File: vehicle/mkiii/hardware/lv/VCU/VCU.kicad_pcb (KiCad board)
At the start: 2 copper layers, 0 parts

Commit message: Resolved some "footprint not exist" issues
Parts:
- added C1: C_0.1uF, OEM:C_0603_1608Metric, F.Cu at (99.6, 103.5)
- added C10: C_0.1uF, OEM:C_0603_1608Metric, F.Cu at (104.7, 67.2)
- added C11: C_10uF_10V, OEM:C_0603_1608Metric, F.Cu at (104.7, 69.7)
- added C12: C_0.1uF, OEM:C_0603_1608Metric, F.Cu at (104.7, 72.2)
- added C13: C_1uF, OEM:C_0603_1608Metric, F.Cu at (104.7, 74.7)
- added C14: C_0.1uF, OEM:C_0603_1608Metric, F.Cu at (104.7, 77.2)
- added C15: C_0.1uF, OEM:C_0603_1608Metric, F.Cu at (104.7, 79.7)
- added C16: C_0.1uF, OEM:C_0603_1608Metric, F.Cu at (104.7, 82.2)
- added C18: C_0.22uF_50V, OEM:C_0603_1608Metric, F.Cu at (130.1, 92.2)
- added C19: C_0.1uF, OEM:C_0603_1608Metric, F.Cu at (130.1, 94.7)
- added C2: C_10nF, OEM:C_0603_1608Metric, F.Cu at (99.6, 106.0)
- added C20: C_0.1uF, OEM:C_0603_1608Metric, F.Cu at (130.1, 97.2)
- added C21: C_1uF_25V, OEM:C_0603_1608Metric, F.Cu at (130.1, 99.7)
- added C22: C_0.1uF_16V, OEM:C_0603_1608Metric, F.Cu at (130.1, 102.2)
- added C23: C_0.1uF, OEM:C_0603_1608Metric, F.Cu at (134.1, 92.2)
- added C24: C_0.1uF, OEM:C_0603_1608Metric, F.Cu at (149.7, 92.2)
- added C25: C_0.1uF, OEM:C_0603_1608Metric, F.Cu at (149.7, 94.7)
- added C26: C_0.1uF_16V, OEM:C_0603_1608Metric, F.Cu at (103.6, 106.0)
- added C27: C_0.1uF, OEM:C_0603_1608Metric, F.Cu at (130.1, 80.2)
- added C28: C_0.1uF, OEM:C_0603_1608Metric, F.Cu at (103.6, 108.5)
- added C29: C_0.1uF, OEM:C_0603_1608Metric, F.Cu at (103.6, 111.0)
- added C3: C_0.1uF, OEM:C_0603_1608Metric, F.Cu at (99.6, 108.5)
- added C30: C_10uF_10V, OEM:C_0603_1608Metric, F.Cu at (130.1, 82.7)
- added C4: C_1uF, OEM:C_0603_1608Metric, F.Cu at (99.6, 111.0)
- added C5: C_4.7uF, OEM:C_0603_1608Metric, F.Cu at (99.6, 113.5)
- added C6: C_0.1uF, OEM:C_0603_1608Metric, F.Cu at (99.6, 116.1)
- added C7: C_30pF, OEM:C_0603_1608Metric, F.Cu at (99.6, 118.6)
- added C8: C_30pF, OEM:C_0603_1608Metric, F.Cu at (103.6, 103.5)
- added C9: C_10uF_10V, OEM:C_0603_1608Metric, F.Cu at (130.1, 77.6)
- added D1: MOTOR_ON, OEM:D_0805_2012Metric, F.Cu at (111.8, 113.4)
- added D10: D_36V_500mW, OEM:D_SOD-123, F.Cu at (105.6, 98.6)
- added D11: BSPD_TRIP_LED, OEM:D_0805_2012Metric, F.Cu at (122.5, 77.9)
- added D13: D_Blue_LED, OEM:D_0805_2012Metric, F.Cu at (139.5, 115.7)
- added D14: HEARTBEAT, OEM:D_0805_2012Metric, F.Cu at (120.7, 119.5)
- added D15: D_Blue_LED, OEM:D_0805_2012Metric, F.Cu at (139.5, 118.7)
- added D2: BRAKES, OEM:D_0805_2012Metric, F.Cu at (111.8, 116.5)
- added D3: BSPD_TRIP, OEM:D_0805_2012Metric, F.Cu at (111.8, 119.5)
- added D4: HEARTBEAT, OEM:D_0805_2012Metric, F.Cu at (116.3, 113.4)
- added D5: 5V, OEM:D_0805_2012Metric, F.Cu at (116.3, 116.5)
- added D6: 3V3, OEM:D_0805_2012Metric, F.Cu at (116.3, 119.5)
- added D7: MISO, OEM:D_0805_2012Metric, F.Cu at (120.7, 113.4)
- added D8: MOSI, OEM:D_0805_2012Metric, F.Cu at (120.7, 116.5)
- added D9: D_Amber_LED, OEM:D_0805_2012Metric, F.Cu at (122.5, 74.9)
- added F1: F_500mA_8V, OEM:Fuse_1206_3216Metric, F.Cu at (147.2, 78.0)
- added F2: F_500mA_8V, OEM:Fuse_1206_3216Metric, F.Cu at (147.2, 81.3)
- added H1: H_MountingHole, OEM:H_MountingHole, F.Cu at (140.3, 79.6)
- added J1: J_Programming_Pin_Header, OEM:J_Programming_Pin_Header_Keyed, F.Cu at (111.9, 104.5)
- added J2: J_PCIe_x1, OEM:J_PCIe_x1_Key, F.Cu at (129.8, 71.9)
- added K1: K_10A_5V, OEM:G5Q1A4DC5 (K_SPST-NO_10A_5V_TH - G5Q-1A4-DC5), F.Cu at (105.5, 94.0)
- added Q1: SSM3K333R,LF, OEM:SOT-23-3, F.Cu at (100.1, 68.3)
- added Q2: SSM3K333R,LF, OEM:SOT-23-3, F.Cu at (100.1, 73.0)
- added Q3: SSM3K333R,LF, OEM:SOT-23-3, F.Cu at (142.7, 105.3)
- added Q5: SSM3K333R,LF, OEM:SOT-23-3, F.Cu at (134.7, 116.6)
- added Q6: SSM3K333R,LF, OEM:SOT-23-3, F.Cu at (134.7, 121.2)
- added R1: R_200, OEM:R_0603_1608Metric, F.Cu at (103.6, 113.5)
- added R10: R_100k, OEM:R_0603_1608Metric, F.Cu at (108.7, 69.7)
- added R11: R_1k, OEM:R_0603_1608Metric, F.Cu at (108.7, 72.2)
- added R12: R_71.5k, OEM:R_0603_1608Metric, F.Cu at (108.7, 74.7)
- added R13: R_10k, OEM:R_0603_1608Metric, F.Cu at (108.7, 77.2)
- added R14: R_10k, OEM:R_0603_1608Metric, F.Cu at (108.7, 79.7)
- added R15: R_10k, OEM:R_0603_1608Metric, F.Cu at (108.7, 82.2)
- added R16: R_100k, OEM:R_0603_1608Metric, F.Cu at (112.7, 67.2)
- added R17: R_10k, OEM:R_0603_1608Metric, F.Cu at (112.7, 69.7)
- added R18: R_1k, OEM:R_0603_1608Metric, F.Cu at (112.7, 72.2)
- added R19: R_10k, OEM:R_0603_1608Metric, F.Cu at (112.7, 74.7)
- added R2: R_200, OEM:R_0603_1608Metric, F.Cu at (103.6, 116.1)
- added R21: R_75k, OEM:R_0603_1608Metric, F.Cu at (134.1, 94.7)
- added R22: R_576, OEM:R_0603_1608Metric, F.Cu at (134.1, 97.2)
- added R23: R_100, OEM:R_0603_1608Metric, F.Cu at (134.1, 99.7)
- added R24: R_10k, OEM:R_0603_1608Metric, F.Cu at (134.1, 102.2)
- added R25: R_1k, OEM:R_0603_1608Metric, F.Cu at (138.1, 92.2)
- added R26: R_10k, OEM:R_0603_1608Metric, F.Cu at (138.1, 94.7)
- added R27: R_10k, OEM:R_0603_1608Metric, F.Cu at (138.1, 97.2)
- added R28: R_10k, OEM:R_0603_1608Metric, F.Cu at (138.1, 99.7)
- added R3: R_200, OEM:R_0603_1608Metric, F.Cu at (103.6, 118.6)
- added R32: R_3k, OEM:R_0603_1608Metric, F.Cu at (130.1, 115.4)
- added R33: R_100k, OEM:R_0603_1608Metric, F.Cu at (130.1, 118.0)
- added R34: R_10k, OEM:R_0603_1608Metric, F.Cu at (130.1, 120.5)
- added R35: R_1M, OEM:R_0603_1608Metric, F.Cu at (149.7, 97.2)
- added R36: R_0, OEM:R_0603_1608Metric, F.Cu at (149.7, 99.7)
- added R37: R_2.2k, OEM:R_0603_1608Metric, F.Cu at (149.7, 102.2)
- added R38: R_1M, OEM:R_0603_1608Metric, F.Cu at (149.7, 104.7)
- added R39: R_120, OEM:R_0603_1608Metric, F.Cu at (107.6, 116.1)
- added R4: R_200, OEM:R_0603_1608Metric, F.Cu at (107.6, 103.5)
- added R40: R_0, OEM:R_0603_1608Metric, F.Cu at (149.7, 107.2)
- added R41: R_2.2k, OEM:R_0603_1608Metric, F.Cu at (149.7, 109.8)
- added R42: R_10k, OEM:R_0603_1608Metric, F.Cu at (130.1, 85.2)
- added R43: R_10k, OEM:R_0603_1608Metric, F.Cu at (130.1, 87.7)
- added R44: R_5.1k, OEM:R_0603_1608Metric, F.Cu at (134.1, 77.6)
- added R45: R_10k, OEM:R_0603_1608Metric, F.Cu at (134.1, 80.2)
- added R46: R_200, OEM:R_0603_1608Metric, F.Cu at (134.1, 82.7)
- added R47: R_5.1k, OEM:R_0603_1608Metric, F.Cu at (134.1, 85.2)
- added R48: R_10k, OEM:R_0603_1608Metric, F.Cu at (134.1, 87.7)
- added R49: R_200, OEM:R_0603_1608Metric, F.Cu at (107.6, 118.6)
- added R5: R_1k, OEM:R_0603_1608Metric, F.Cu at (107.6, 106.0)
- added R50: R_3k, OEM:R_0603_1608Metric, F.Cu at (130.1, 123.0)
- added R51: R_100k, OEM:R_0603_1608Metric, F.Cu at (130.1, 125.5)
- added R52: R_10k, OEM:R_0603_1608Metric, F.Cu at (130.1, 128.0)
- added R6: R_200, OEM:R_0603_1608Metric, F.Cu at (107.6, 108.5)
- added R7: R_200, OEM:R_0603_1608Metric, F.Cu at (107.6, 111.0)
- added R8: R_200, OEM:R_0603_1608Metric, F.Cu at (107.6, 113.5)
- added R9: R_100k, OEM:R_0603_1608Metric, F.Cu at (108.7, 67.2)
- added SW1: SW_0.05A_12V, OEM:B3U-1000P (SW_SPST_0.05A_12V_SMD - B3U-1000P), F.Cu at (122.8, 67.8)
- added SW2: SW_0.05A_12V, OEM:B3U-1000P (SW_SPST_0.05A_12V_SMD - B3U-1000P), F.Cu at (122.8, 71.5)
- added TP1: 5V, OEM:TP_Hook_SMD, F.Cu at (112.3, 123.0)
- added TP10: TP_SMD, OEM:TP_Hook_SMD, F.Cu at (154.4, 92.9)
- added TP11: TP_SMD, OEM:TP_Hook_SMD, F.Cu at (154.4, 96.9)
- added TP12: TP_SMD, OEM:TP_Hook_SMD, F.Cu at (134.9, 125.4)
- added TP2: GND, OEM:TP_Hook_SMD, F.Cu at (112.3, 127.0)
- added TP3: TP_SMD, OEM:TP_Hook_SMD, F.Cu at (117.5, 67.9)
- added TP4: TP_SMD, OEM:TP_Hook_SMD, F.Cu at (117.5, 71.9)
- added TP5: TP_SMD, OEM:TP_Hook_SMD, F.Cu at (117.5, 75.9)
- added TP6: TP_SMD, OEM:TP_Hook_SMD, F.Cu at (142.9, 92.9)
- added TP7: TP_SMD, OEM:TP_Hook_SMD, F.Cu at (142.9, 96.9)
- added TP8: TP_SMD, OEM:TP_Hook_SMD, F.Cu at (142.9, 100.9)
- added U1: STM32G441CBT6, OEM:LQFP-48_7x7mm_P0.5mm, F.Cu at (103.2, 125.5)
- added U10: MCP6001T-I/LT, OEM:SOT-353_SC-70-5, F.Cu at (153.8, 100.9)
- added U11: MCP6001T-I/LT, OEM:SOT-353_SC-70-5, F.Cu at (153.8, 104.9)
- added U12: MCP2561-E_SN, OEM:SOIC-8_3.9x4.9mm_P1.27mm, F.Cu at (119.3, 124.4)
- added U13: MCP6001T-I/LT, OEM:SOT-353_SC-70-5, F.Cu at (146.5, 85.0)
- added U2: SN74LVC1G08DBVR, OEM:SOT-23-5, F.Cu at (100.1, 77.6)
- added U3: MCP6001T-I/LT, OEM:SOT-353_SC-70-5, F.Cu at (122.4, 81.4)
- added U4: SN74LVC1G02DBVR, OEM:SOT-23-5, F.Cu at (100.1, 82.2)
- added U5: SN74LVC1G02DBVR, OEM:SOT-23-5, F.Cu at (100.1, 86.8)
- added U6: SN74LVC1G32DBVR, OEM:SOT-23-5, F.Cu at (142.7, 110.0)
- added U7: MCP6001T-I/LT, OEM:SOT-353_SC-70-5, F.Cu at (130.2, 105.5)
- added U8: MCP6001T-I/LT, OEM:SOT-353_SC-70-5, F.Cu at (130.2, 109.4)
- added Y1: X_16MHz_18pF, OEM:FA238160000MBC0 (X_16MHz_18pF_SMD - FA-238_16.0000MB-C0), F.Cu at (120.1, 105.2)
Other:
- board outline added: 20.3 x 8.4 mm

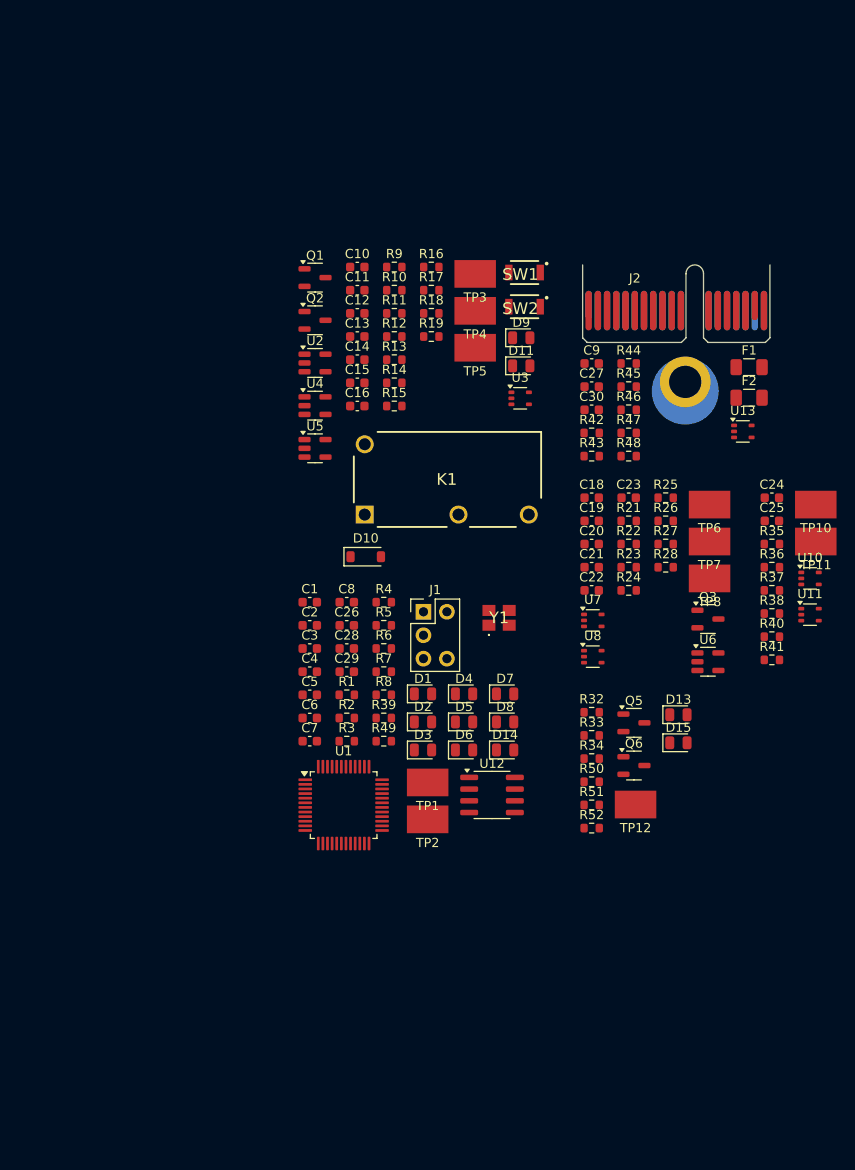
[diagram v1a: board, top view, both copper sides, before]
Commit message: Layout completed, review required
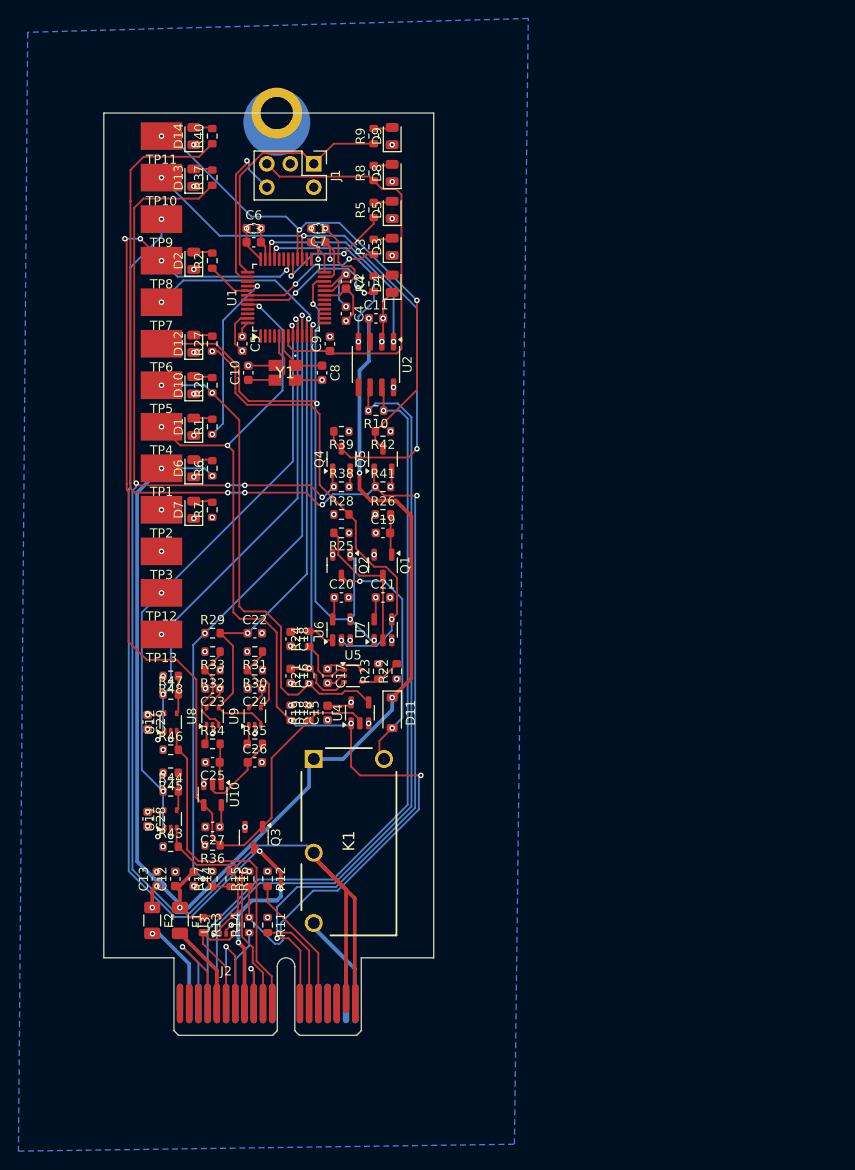
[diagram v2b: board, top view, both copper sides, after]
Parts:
- removed SW1, SW2: SW_0.05A_12V, OEM:B3U-1000P (SW_SPST_0.05A_12V_SMD - B3U-1000P)
- added TP11: TP_SMD, OEM:TP_Hook_SMD, F.Cu at (83.5, 53.0)
- added TP2: 3V3, OEM:TP_Hook_SMD, F.Cu at (83.5, 93.5)
- D5: renamed from D14; value HEARTBEAT -> THROTTLE_DISABLE
- D8: renamed from D7; value MISO -> NRST
- D9: renamed from D8; value MOSI -> SWDIO
- moved J2 87.2 mm to (85.5, 147.0)
- moved F1 86.0 mm to (85.5, 138.0), turned to -90 degrees
- moved F2 86.0 mm to (82.5, 138.0), turned to -90 degrees
- moved TP10 85.2 mm to (83.5, 57.5)
- moved D14 81.8 mm to (87.0, 53.0), turned to 90 degrees
- moved D13 80.7 mm to (87.0, 57.5), turned to 90 degrees
- moved U3 77.4 mm to (90.5, 138.5), turned to 90 degrees
- moved R37 77.3 mm to (89.0, 57.5), turned to 90 degrees
- moved C28 76.1 mm to (82.0, 127.0), turned to -90 degrees
- moved R40 74.8 mm to (89.0, 53.0), turned to 90 degrees
- moved U11 74.0 mm to (84.5, 127.0), turned to 90 degrees
- moved R43 72.9 mm to (84.5, 130.0)
- moved C12 71.8 mm to (85.0, 133.5), turned to 90 degrees
- moved TP13 71.6 mm to (83.5, 107.0)
- moved TP12 71.5 mm to (83.5, 102.5)
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- renumbered C29 to C1, C8 to C10, C26 to C11, C9 to C12, C30 to C13, C27 to C14, C10 to C15, C11 to C16, C12 to C17, C13 to C18, C14 to C19, C15 to C20, C16 to C21, C18 to C22, C19 to C23, C20 to C24, C21 to C25, C22 to C26, C23 to C27, C24 to C28, C25 to C29, C1 to C3, C3 to C5, C5 to C6, C28 to C7, C7 to C8, C6 to C9, D9 to D10, D10 to D11, D11 to D12, D15 to D13, D13 to D14, D5 to D6, D6 to D7, Q6 to Q4, R39 to R10, R45 to R11, R46 to R12, R42 to R13, R47 to R14, R48 to R15, R44 to R16, R43 to R17, R9 to R18, R10 to R19, R11 to R20, R12 to R21, R13 to R22, R14 to R23, R15 to R24, R16 to R25, R17 to R26, R18 to R27, R19 to R28, R21 to R29, R22 to R30, R23 to R31, R24 to R32, R25 to R33, R26 to R34, R27 to R35, R28 to R36, R50 to R37, R51 to R38, R52 to R39, R32 to R40, R33 to R41, R34 to R42, R35 to R43, R40 to R44, R41 to R45, R38 to R46, R36 to R47, R37 to R48, R49 to R5, R5 to R6, R6 to R7, R7 to R8, R8 to R9, TP12 to TP10, TP10 to TP12, TP11 to TP13, TP2 to TP3, TP3 to TP4, TP4 to TP5, TP5 to TP6, TP6 to TP7, TP7 to TP8, TP8 to TP9, U6 to U10, U10 to U11, U11 to U12, U12 to U2, U13 to U3, U2 to U4, U3 to U5, U4 to U6, U5 to U7, U7 to U8, U8 to U9
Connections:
- U1 pad 1: +3V3 -> unconnected-(U1-VBAT-Pad1)
- U1 pad 43: /Microcontroller - STM32G441CBT6 (page 2)/HEARTBEAT -> /Microcontroller - STM32G441CBT6 (page 2)/HEARTBEAT_LED
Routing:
- net /BSPD/BSPD_RELAY_OUT: track 0.00 -> 166.7 mm, vias 0 -> 5
- net +5V: track 0.00 -> 150.7 mm, vias 0 -> 6
- net /PCIe x1 Connector/SS_INERTIA_SWITCH: track 0.00 -> 145.2 mm, vias 0 -> 6
- net /BSPD/BRAKELIGHT_LL: track 0.00 -> 118.3 mm, vias 0 -> 4
- net /BSPD/MOTOR_CURRENT_SENSE: track 0.00 -> 115.7 mm, vias 0 -> 7
- net /BrakeLight/BRAKELIGHT_CONN: track 0.00 -> 114.4 mm, vias 0 -> 4
- net /Microcontroller - STM32G441CBT6 (page 2)/CAN_-: track 0.00 -> 85.3 mm, vias 0 -> 1
- net /Microcontroller - STM32G441CBT6 (page 2)/CAN_+: track 0.00 -> 82.7 mm, vias 0 -> 1
- net GND: track 0.00 -> 80.6 mm, vias 0 -> 69
- net /BrakeLight/BRAKE_PRESS_SENSE_FILTERED: track 0.00 -> 75.6 mm, vias 0 -> 3
- net /BSPD/BSPD_LL: track 0.00 -> 72.8 mm, vias 0 -> 5
- net /BrakeLight/BRAKE_PRESS_SENSE: track 0.00 -> 72.0 mm, vias 0 -> 3
- net /Microcontroller - STM32G441CBT6 (page 2)/OUTPUT_THROTTLE_1: track 0.00 -> 65.9 mm, vias 0 -> 4
- net /Microcontroller - STM32G441CBT6 (page 2)/BSPD_SHUTDOWN_SENSE: track 0.00 -> 62.6 mm, vias 0 -> 3
- net /Microcontroller - STM32G441CBT6 (page 2)/SS_INERTIA_OUTPUT: track 0.00 -> 57.2 mm, vias 0 -> 3
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- added copper zone on In2.Cu, net +3V3
- added copper zone on B.Cu, net GND
- added copper zone on In1.Cu, net GND
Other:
- board size 20.3 x 8.4 mm -> 35.8 x 91.6 mm
- copper layers 2 -> 4

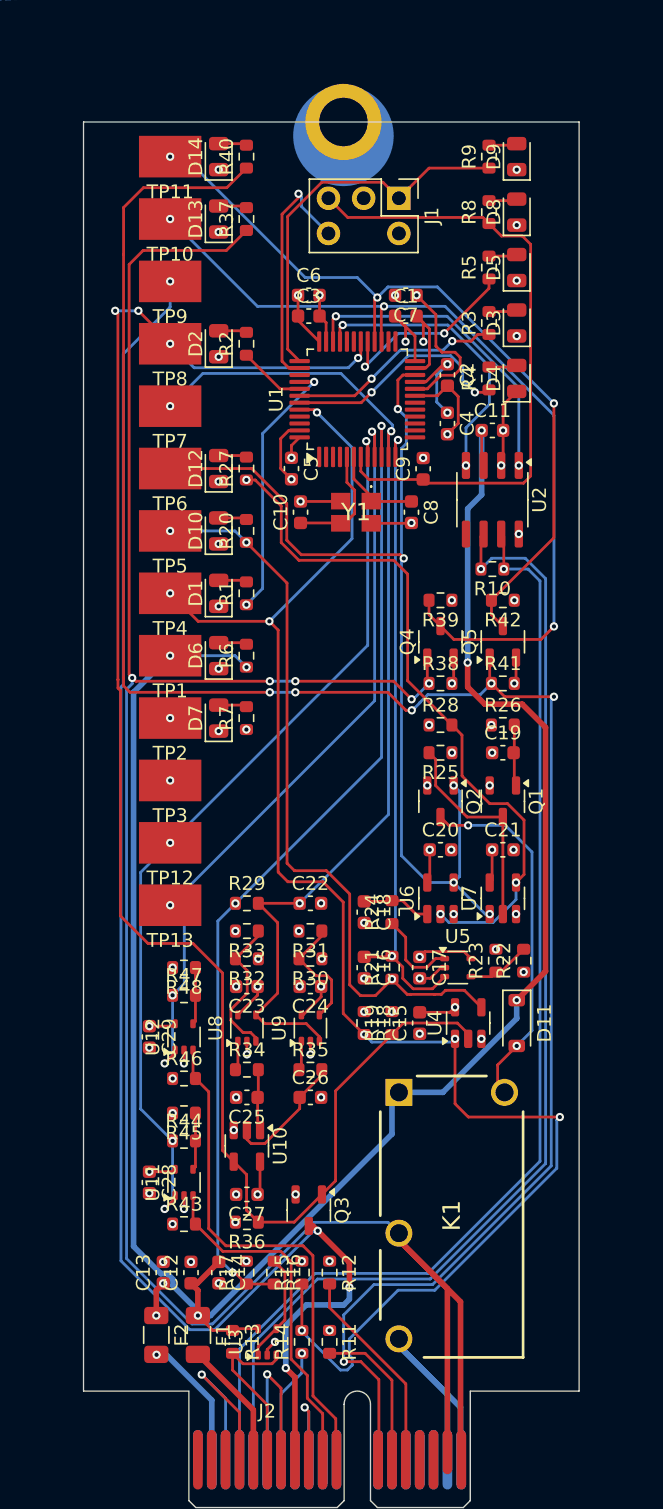
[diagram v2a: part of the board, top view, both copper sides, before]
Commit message: Final PCB layout after adding silkscreen and icon
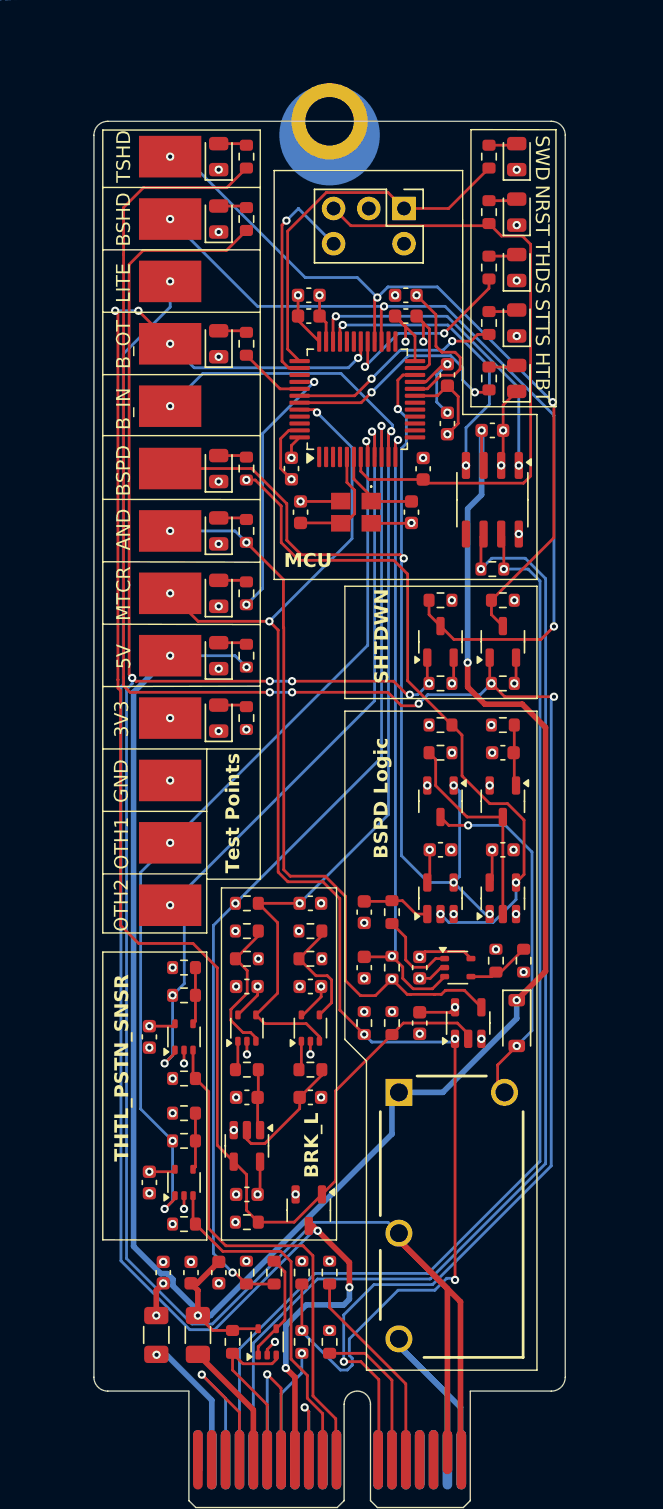
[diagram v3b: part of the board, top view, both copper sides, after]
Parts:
- added G***: LOGO, LOGO, B.Cu at (95.7, 75.1)
- moved H1 1.00 mm to (95.0, 50.4)
- moved J1 0.83 mm to (100.4, 56.7)
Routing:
- net /BSPD/MOTOR_CURRENT_SENSE: track 115.7 -> 106.1 mm
- net /Microcontroller - STM32G441CBT6 (page 2)/SWCLK: track 17.9 -> 16.6 mm
- net /Microcontroller - STM32G441CBT6 (page 2)/SWDIO: track 27.7 -> 27.1 mm
- net /Microcontroller - STM32G441CBT6 (page 2)/NRST: track 46.3 -> 45.7 mm
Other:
- board size 35.8 x 91.6 mm -> 34 x 91.6 mm
- board text added: "3V3"
- board text added: "5V"
- board text added: "AND"
- board text added: "BRK_L"
- board text added: "BSHD"
- board text added: "BSPD"
- board text added: "BSPD Logic"
- board text added: "B_IN"
- board text added: "B_OT"
- board text added: "GND"
- board text added: "HTBT"
- board text added: "LITE"
- board text added: "MCU"
- board text added: "MTCR"
- board text added: "NRST"
- board text added: "OTH1"
- board text added: "OTH2"
- board text added: "SHTDWN"
- board text added: "STTS"
- board text added: "SWD"
- board text added: "THDS"
- board text added: "THTL_PSTN_SNSR"
- board text added: "TSHD"
- board text added: "Test Points"

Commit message: Minor ERC Fixes in Schematics; Minor Silkscreen Changes; Addedc Subteam Layout; Added Production Files.
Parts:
- added G***: LOGO, LOGO, B.Cu at (97.4, 102.3)
- added REF**: OEM_Logo_8mm, OEM:OEM_Logo_8mm, B.Cu at (83.0, 137.1)
- added kibuzzard-6983BE89: G***, kibuzzard-6983BE89, B.Cu at (80.2, 124.8)
- added kibuzzard-6983C564: G***, kibuzzard-6983C564, B.Cu at (85.8, 123.0)
- added kibuzzard-6983C636: G***, kibuzzard-6983C636, B.Cu at (83.0, 128.3)
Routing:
- net /BrakeLight/BRAKELIGHT_CONN: track 114.4 -> 113.3 mm
- net /Microcontroller - STM32G441CBT6 (page 2)/SWCLK: track 16.6 -> 15.8 mm
- net +3V3: track 56.1 -> 55.5 mm
- net Net-(R27-Pad1): vias 3 -> 2
- net Net-(R20-Pad1): vias 3 -> 2
- net /BSPD/MOTOR_CURRENT_SENSE: vias 7 -> 6
